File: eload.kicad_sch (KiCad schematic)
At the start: 41 parts, among them J1 Device Power, J2 Input, J3 JST Header, J4 SWD Header, J6 JST Header, Q1 TIP122, SW1 SW_Push, SW2 RotaryEncoder_Switch, U1 LM1117DT-3.3, U2 STM32F103CBT6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

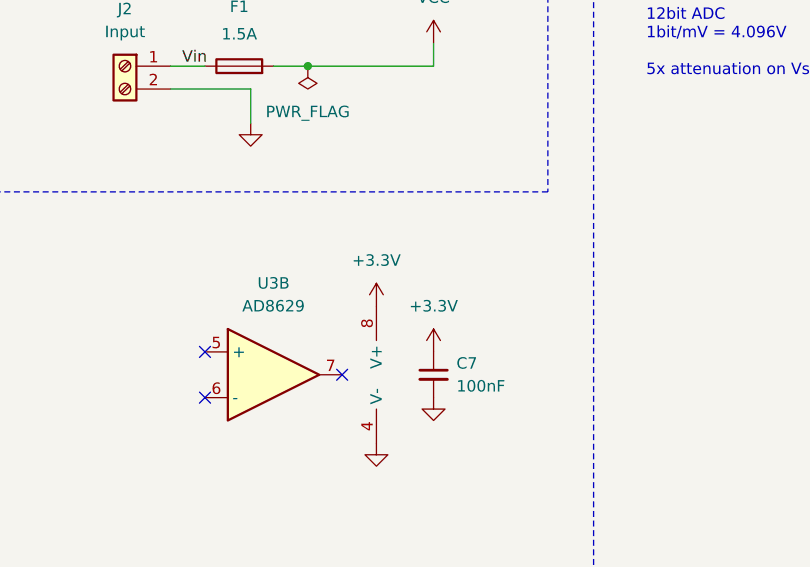
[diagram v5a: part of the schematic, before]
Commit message: Move AD8629 power rail to 5V
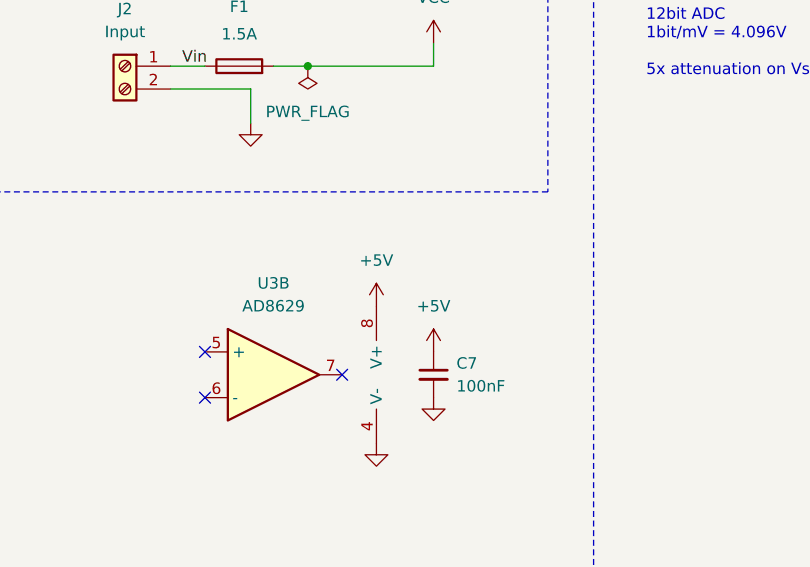
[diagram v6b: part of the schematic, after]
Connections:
- net +3.3V: no longer C7.1, U3.8 (V+)
- net +5V: now also C7.1, U3.8 (V+)
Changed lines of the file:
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@@
 	)
 	(symbol
+		(lib_id "power:+5V")
+		(at 154.94 71.12 0)
+		(unit 1)
+		(exclude_from_sim no)
+		(in_bom yes)
+		(on_board yes)
+		(dnp no)
+		(fields_autoplaced yes)
+		(property "Reference" "#PWR029"
+			(at 154.94 74.93 0)
+			(effects
+				(font
+					(size 1.27 1.27)
+				)
+				(hide yes)
+			)
+		)
+		(property "Value" "+5V"
+			(at 154.94 66.04 0)
+			(effects
+				(font
+					(size 1.27 1.27)
+				)
+			)
+		)
+		(property "Footprint" ""
+			(at 154.94 71.12 0)
+			(effects
+				(font
+					(size 1.27 1.27)
+				)
+				(hide yes)
+			)
+		)
+		(property "Datasheet" ""
+			(at 154.94 71.12 0)
+			(effects
+				(font
+					(size 1.27 1.27)
+				)
+				(hide yes)
+			)
+		)
+		(property "Description" "Power symbol creates a global label with name \"+5V\""
+			(at 154.94 71.12 0)
+			(effects
+				(font
+					(size 1.27 1.27)
+				)
+				(hide yes)
+			)
+		)
+		(pin "1"
+		)
+		(instances
+			(project "eload"
+				(path "/6911506d-905a-4c6c-8722-d6c9741e8402"
+					(reference "#PWR029")
+					(unit 1)
+				)
+			)
+		)
+	)
+	(symbol
 		(lib_id "power:GND")
 		(at 264.16 91.44 0)
@@
 	)
 	(symbol
-		(lib_id "power:+3.3V")
-		(at 148.59 66.04 0)
-		(unit 1)
-		(exclude_from_sim no)
-		(in_bom yes)
-		(on_board yes)
-		(dnp no)
-		(fields_autoplaced yes)
-		(property "Reference" "#PWR023"
-			(at 148.59 69.85 0)
-			(effects
-				(font
-					(size 1.27 1.27)
-				)
-				(hide yes)
-			)
-		)
-		(property "Value" "+3.3V"
-			(at 148.59 60.96 0)
-			(effects
-				(font
-					(size 1.27 1.27)
-				)
-			)
-		)
-		(property "Footprint" ""
-			(at 148.59 66.04 0)
-			(effects
-				(font
-					(size 1.27 1.27)
-				)
-				(hide yes)
-			)
-		)
-		(property "Datasheet" ""
-			(at 148.59 66.04 0)
-			(effects
-				(font
-					(size 1.27 1.27)
-				)
-				(hide yes)
-			)
-		)
-		(property "Description" "Power symbol creates a global label with name \"+3.3V\""
-			(at 148.59 66.04 0)
-			(effects
-				(font
-					(size 1.27 1.27)
-				)
-				(hide yes)
-			)
-		)
-		(pin "1"
-		)
-		(instances
-			(project "eload"
-				(path "/6911506d-905a-4c6c-8722-d6c9741e8402"
-					(reference "#PWR023")
-					(unit 1)
-				)
-			)
-		)
-	)
-	(symbol
 		(lib_id "Device:R_Small")
 		(at 226.06 59.69 0)
@@
 	(symbol
 		(lib_id "power:+3.3V")
-		(at 154.94 71.12 0)
-		(unit 1)
-		(exclude_from_sim no)
-		(in_bom yes)
-		(on_board yes)
-		(dnp no)
-		(fields_autoplaced yes)
-		(property "Reference" "#PWR029"
-			(at 154.94 74.93 0)
-			(effects
-				(font
-					(size 1.27 1.27)
-				)
-				(hide yes)
-			)
-		)
-		(property "Value" "+3.3V"
-			(at 154.94 66.04 0)
-			(effects
-				(font
-					(size 1.27 1.27)
-				)
-			)
-		)
-		(property "Footprint" ""
-			(at 154.94 71.12 0)
-			(effects
-				(font
-					(size 1.27 1.27)
-				)
-				(hide yes)
-			)
-		)
-		(property "Datasheet" ""
-			(at 154.94 71.12 0)
-			(effects
-				(font
-					(size 1.27 1.27)
-				)
-				(hide yes)
-			)
-		)
-		(property "Description" "Power symbol creates a global label with name \"+3.3V\""
-			(at 154.94 71.12 0)
-			(effects
-				(font
-					(size 1.27 1.27)
-				)
-				(hide yes)
-			)
-		)
-		(pin "1"
-		)
-		(instances
-			(project "eload"
-				(path "/6911506d-905a-4c6c-8722-d6c9741e8402"
-					(reference "#PWR029")
-					(unit 1)
-				)
-			)
-		)
-	)
-	(symbol
-		(lib_id "power:+3.3V")
 		(at 81.28 101.6 0)
 		(unit 1)
@@
 					(unit 1)
 				)
+			)
+		)
+	)
+	(symbol
+		(lib_id "power:+5V")
+		(at 148.59 66.04 0)
+		(unit 1)
+		(exclude_from_sim no)
+		(in_bom yes)
+		(on_board yes)
+		(dnp no)
+		(fields_autoplaced yes)
+		(property "Reference" "#PWR023"
+			(at 148.59 69.85 0)
+			(effects
+				(font
+					(size 1.27 1.27)
+				)
+				(hide yes)
+			)
+		)
+		(property "Value" "+5V"
+			(at 148.59 60.96 0)
+			(effects
+				(font
+					(size 1.27 1.27)
+				)
+			)
+		)
+		(property "Footprint" ""
+			(at 148.59 66.04 0)
+			(effects
+				(font
+					(size 1.27 1.27)
+				)
+				(hide yes)
+			)
+		)
+		(property "Datasheet" ""
+			(at 148.59 66.04 0)
+			(effects
+				(font
+					(size 1.27 1.27)
+				)
+				(hide yes)
+			)
+		)
+		(property "Description" "Power symbol creates a global label with name \"+5V\""
+			(at 148.59 66.04 0)
+			(effects
+				(font
+					(size 1.27 1.27)
+				)
+				(hide yes)
+			)
+		)
+		(pin "1"
+		)
+		(instances
+			(project "eload"
+				(path "/6911506d-905a-4c6c-8722-d6c9741e8402"
+					(reference "#PWR023")
+					(unit 1)
+				)

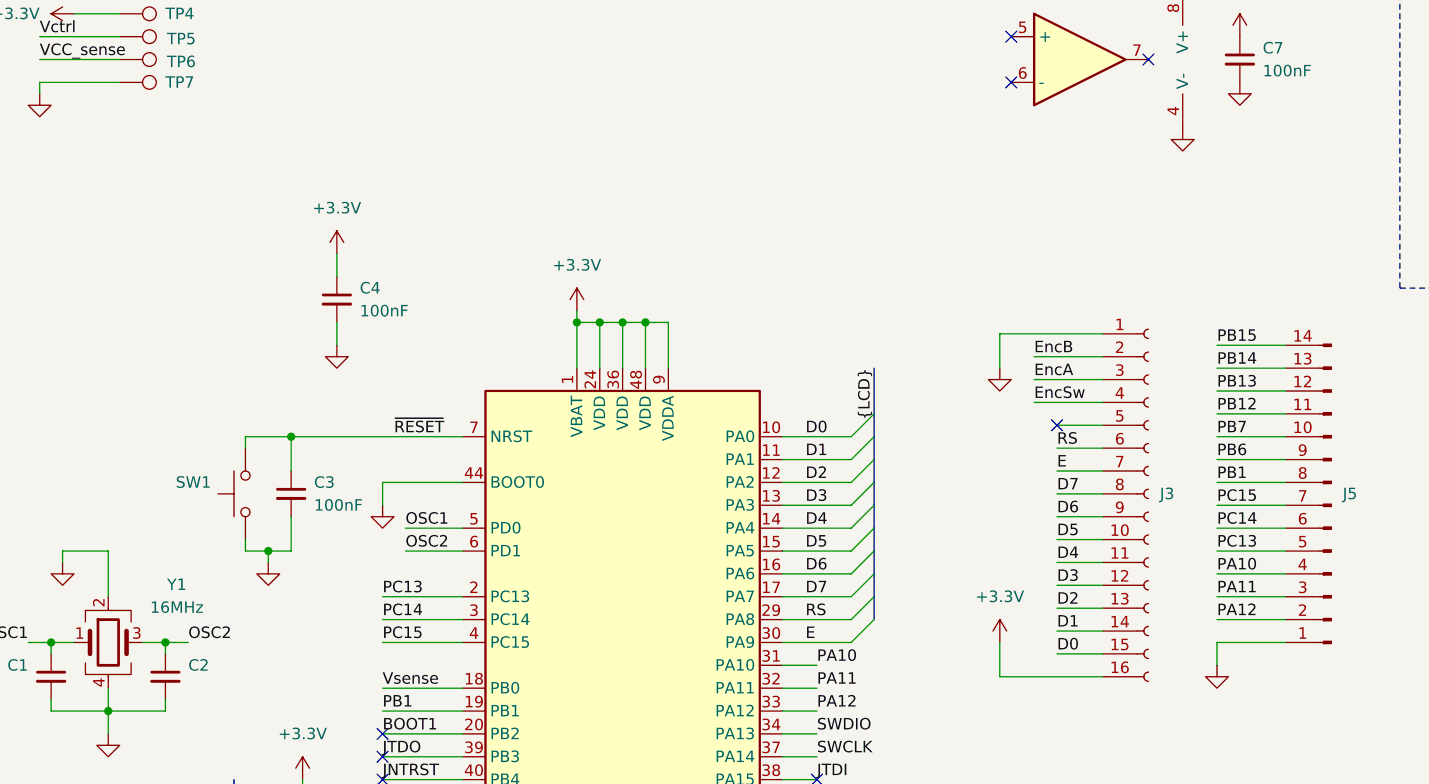
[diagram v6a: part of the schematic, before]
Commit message: Routing power plane for STM32
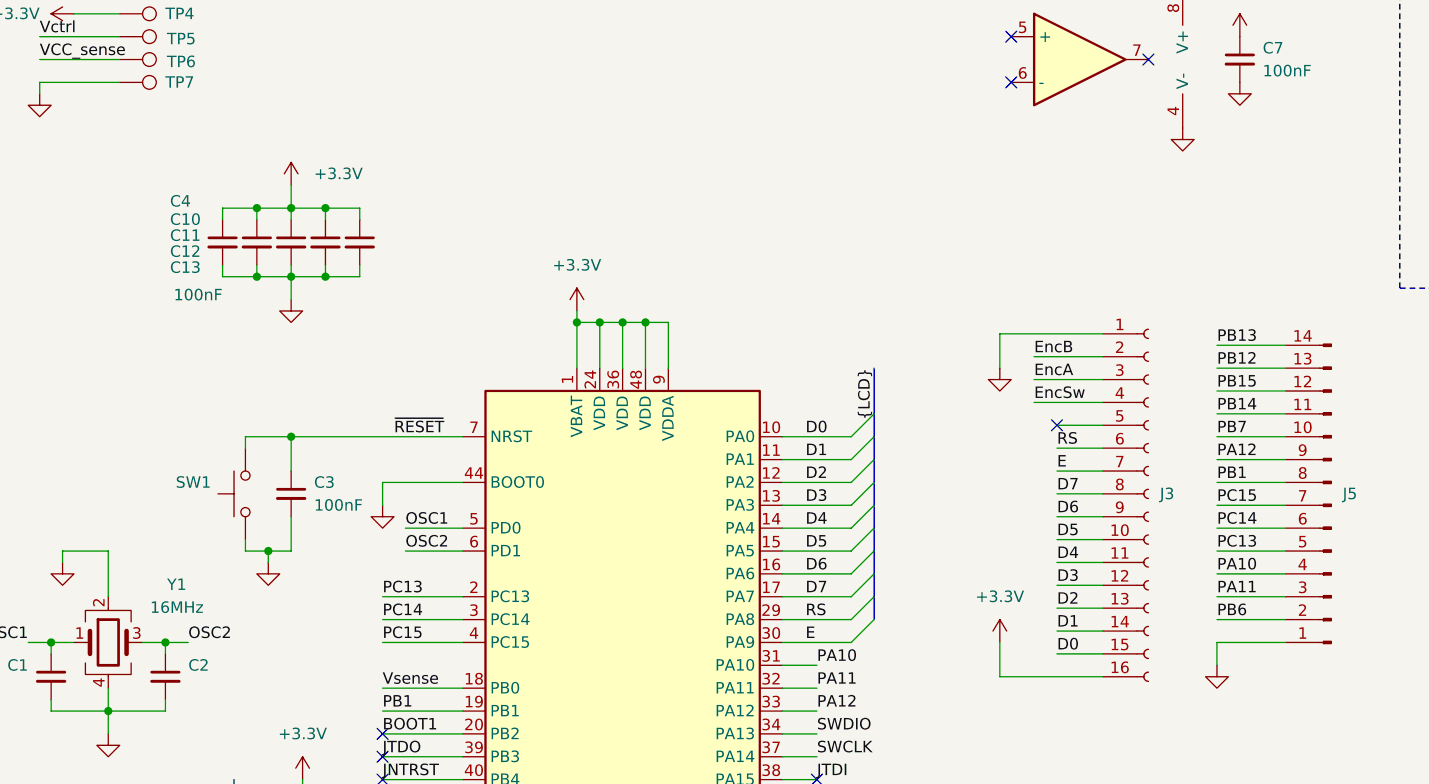
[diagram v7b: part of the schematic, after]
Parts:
- added C10, C11, C12, C13: 100nF, Capacitor_SMD:C_0805_2012Metric_Pad1.18x1.45mm_HandSolder, symbol Device:C_Small
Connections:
- net +3.3V: now also C10.1, C11.1, C12.1, C13.1
- net GND: now also C10.2, C11.2, C12.2, C13.2
- net PA12: now also J5.9 (Pin_9); no longer J5.2 (Pin_2)
- net PB12: now also J5.13 (Pin_13); no longer J5.11 (Pin_11)
- net PB13: now also J5.14 (Pin_14); no longer J5.12 (Pin_12)
- net PB14: now also J5.11 (Pin_11); no longer J5.13 (Pin_13)
- net PB15: now also J5.12 (Pin_12); no longer J5.14 (Pin_14)
- net PB6: now also J5.2 (Pin_2); no longer J5.9 (Pin_9)
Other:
- moved on the sheet: C4

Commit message: Banana connector
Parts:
- J2: footprint TerminalBlock_CUI:TerminalBlock_CUI_TB007-508-02_1x02_P5.08mm_Horizontal -> Connector:Banana_Jack_2Pin
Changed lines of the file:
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@@
 			)
 		)
-		(property "Footprint" "TerminalBlock_CUI:TerminalBlock_CUI_TB007-508-02_1x02_P5.08mm_Horizontal"
+		(property "Footprint" "Connector:Banana_Jack_2Pin"
 			(at 120.65 39.37 0)
 			(effects
